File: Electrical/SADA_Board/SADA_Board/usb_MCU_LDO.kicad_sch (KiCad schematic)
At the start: 12 parts, among them J16 USB_B_Micro, Q2 NVR5198NLT1G, Q3 NVR5198NLT1G, U11 RTQ2520GQW, U12 NCV68261MTWAITBG, U13 NCV68261MTWAITBG

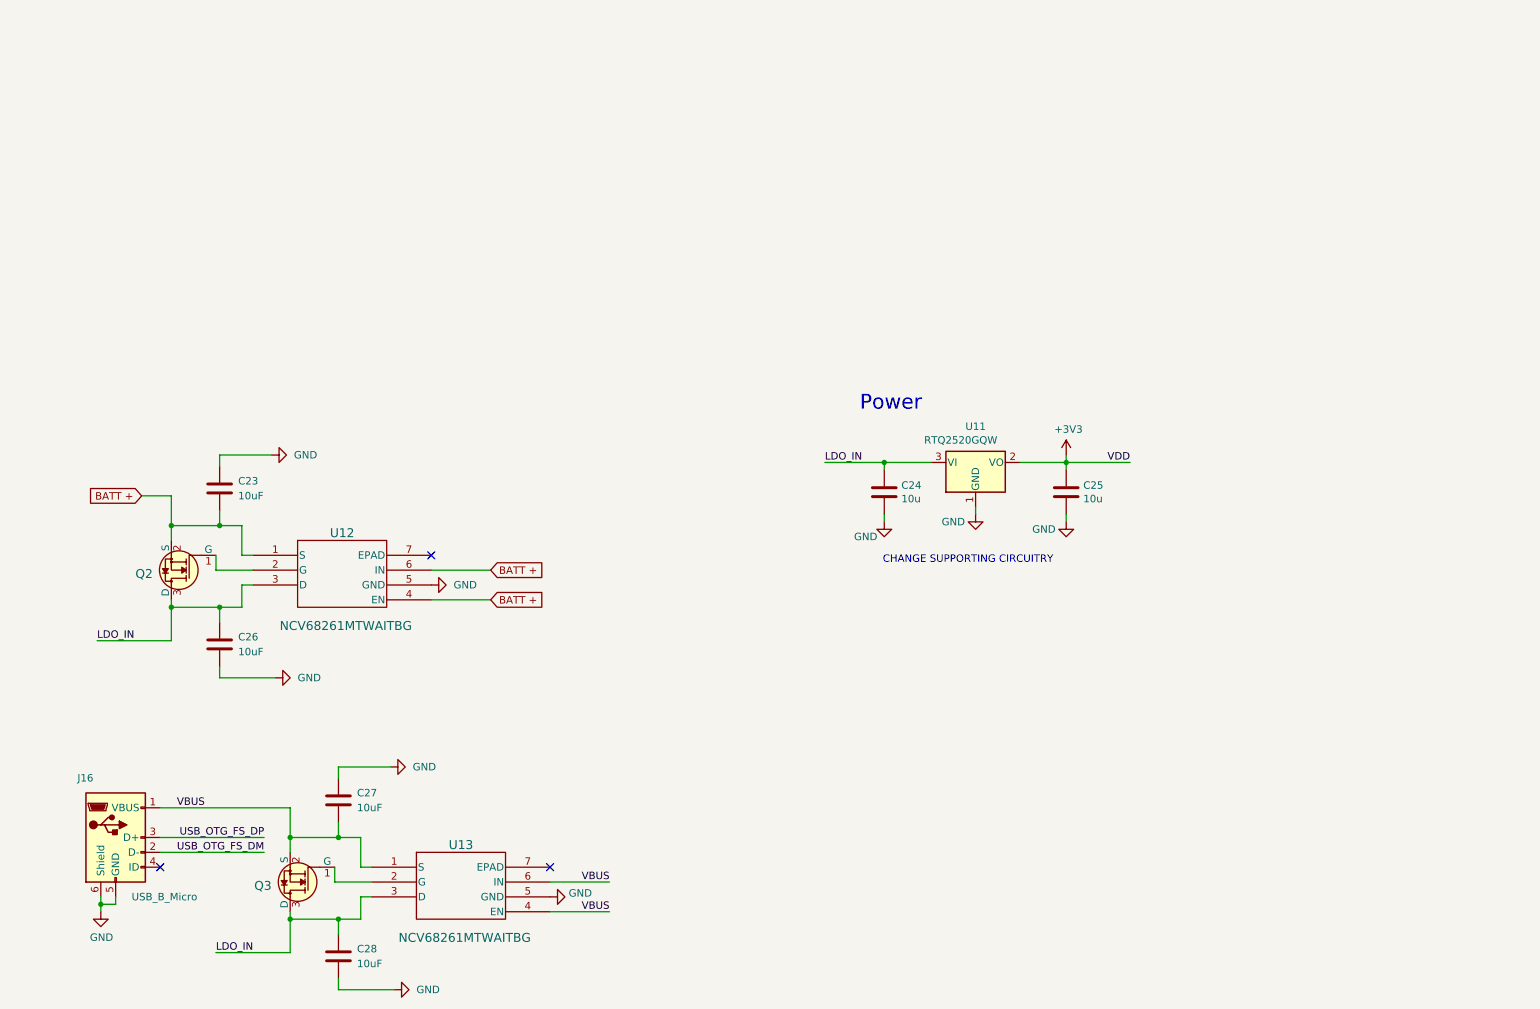
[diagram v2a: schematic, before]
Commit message: Connectors, Oscillator
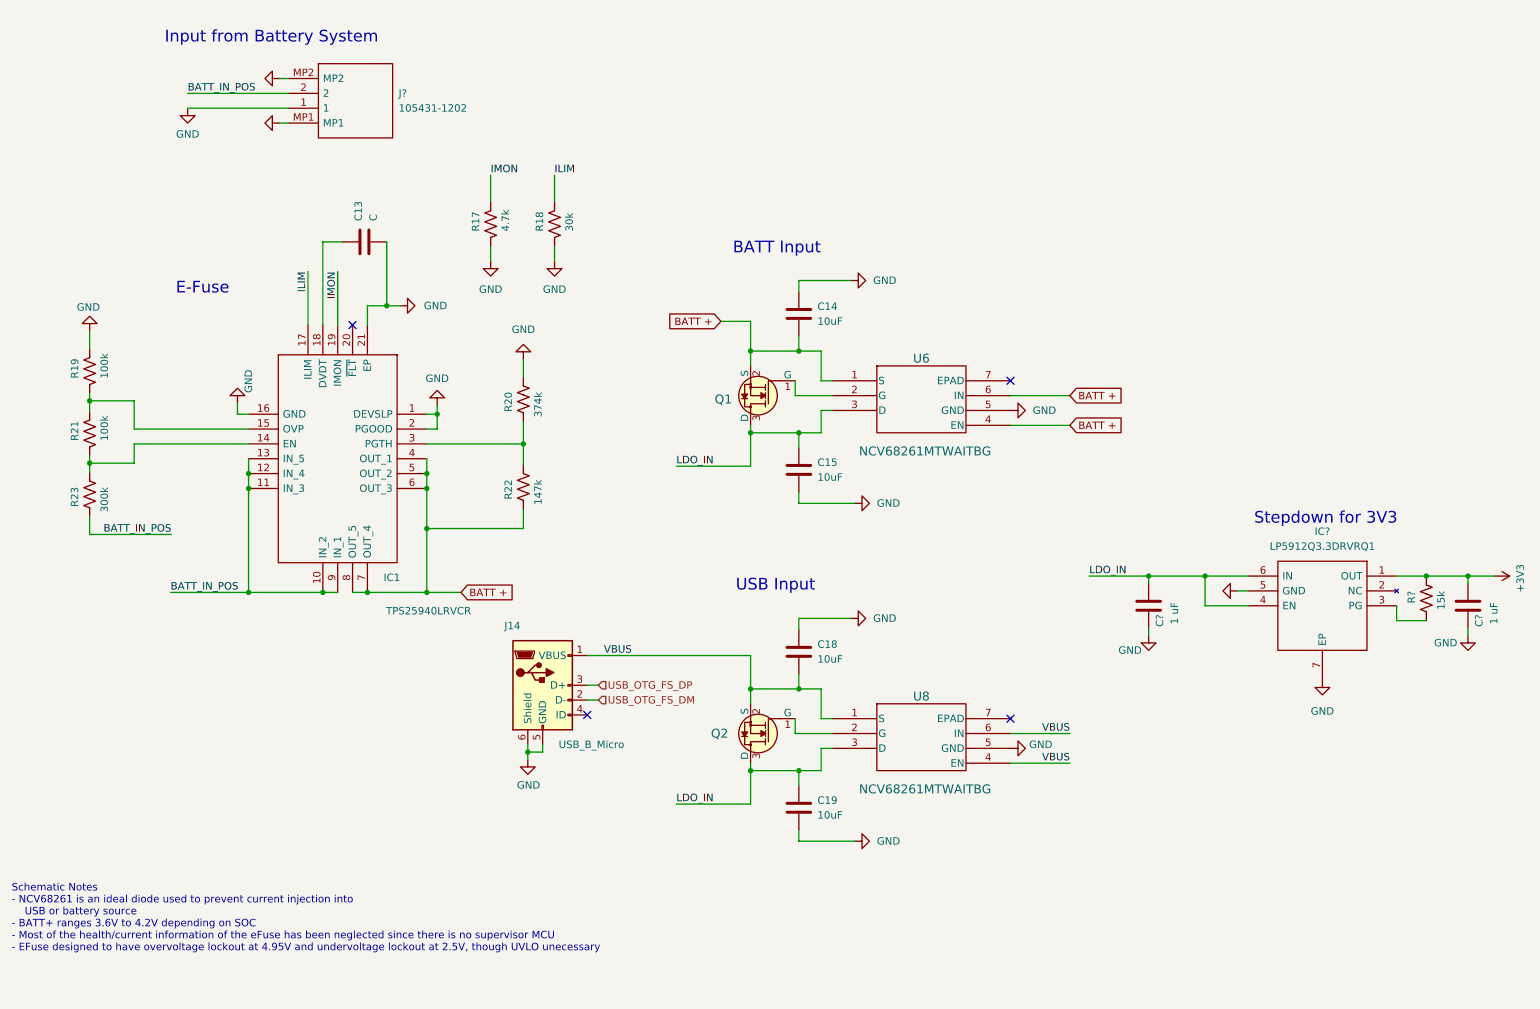
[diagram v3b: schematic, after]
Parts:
- removed C23, C27, C28: 10uF, Capacitor_SMD:C_0603_1608Metric_Pad1.08x0.95mm_HandSolder, symbol Device:C
- removed C24, C25: 10u, Capacitor_SMD:C_0805_2012Metric, symbol Device:C
- removed U11: RTQ2520GQW, symbol Regulator_Linear:NCP1117-3.3_SOT223
- added C13: C, Capacitor_SMD:C_0402_1005Metric, symbol Device:C
- added C14, C18, C19: 10uF, Capacitor_SMD:C_0603_1608Metric, symbol Device:C
- added C? (x2): 1 uF, Capacitor_SMD:C_0603_1608Metric, symbol Device:C
- added IC1: TPS25940LRVCR, QFN50P300X400X80-21N, symbol TPS25940LRVCR:TPS25940LRVCR
- added IC?: LP5912Q3.3DRVRQ1, SON65P200X200X80-7N, symbol LP5912Q3.3DRVRQ1:LP5912Q3.3DRVRQ1
- added J?: 105431-1202, Miles Added:1054311202, symbol molex_105431-1202:105431-1202
- added R17: 4.7k, Resistor_SMD:R_0402_1005Metric, symbol Device:R_US
- added R18: 30k, Resistor_SMD:R_0402_1005Metric, symbol Device:R_US
- added R19, R21: 100k, Resistor_SMD:R_0402_1005Metric, symbol Device:R_US
- added R20: 374k, Resistor_SMD:R_0402_1005Metric, symbol Device:R_US
- added R22: 147k, Resistor_SMD:R_0402_1005Metric, symbol Device:R_US
- added R23: 300k, Resistor_SMD:R_0402_1005Metric, symbol Device:R_US
- added R?: 15k, Resistor_SMD:R_0603_1608Metric, symbol Device:R_US
- C15: renamed from C26; footprint Capacitor_SMD:C_0603_1608Metric_Pad1.08x0.95mm_HandSolder -> Capacitor_SMD:C_0603_1608Metric
- renumbered J16 to J14, Q2 to Q1, Q3 to Q2, U12 to U6, U13 to U8
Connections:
- net +3V3: now also C?.2, IC?.1 (OUT), R?.2
- net BATT +: now also C14.2, IC1.4 (OUT_1), IC1.5 (OUT_2), IC1.6 (OUT_3), IC1.7 (OUT_4), IC1.8 (OUT_5), R22.1
- net GND: now also C13.2, C14.1, C18.1, C19.2, C?.1, C?.1, IC1.1 (DEVSLP), IC1.16 (GND), IC1.2 (PGOOD), IC1.21 (EP), IC?.5 (GND), IC?.7 (EP), J?.1, J?.MP1, J?.MP2, R17.2, R18.2, R19.1, R20.2
- net LDO_IN: now also C19.1, C?.2, IC?.4 (EN), IC?.6 (IN)
- net VBUS: now also C18.2
- new net: C13.1, IC1.18 (DVDT)
- new net: IC1.15 (OVP), R19.2, R21.1
- new net: IC1.14 (EN), R21.2, R23.2
- new net: IC1.3 (PGTH), R20.1, R22.2
- new net: IC?.3 (PG), R?.1
- new net BATT_IN_POS: IC1.10 (IN_2), IC1.11 (IN_3), IC1.12 (IN_4), IC1.13 (IN_5), IC1.9 (IN_1), J?.2, R23.1
- new net ILIM: IC1.17 (ILIM), R18.1
- new net IMON: IC1.19 (IMON), R17.1
- no-connect marks 3 -> 4
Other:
- note added: "BATT Input"
- note added: "E-Fuse"
- note added: "Input from Battery System"
- note added: "Schematic Notes - NCV68261 is an ideal diode used to prevent current injection into USB or battery source - BATT+ ranges 3.6V to 4.2V depending on SOC - Most of the health/current information of the eFuse has been neglected since there is no supervisor MCU - EFuse designed to have overvoltage lockout at 4.95V and undervoltage lockout at 2.5V, though UVLO unecessary"
- note added: "Stepdown for 3V3"
- note added: "USB Input"
- note removed: "CHANGE SUPPORTING CIRCUITRY"
- note removed: "Power"
- moved on the sheet: C15, J14, Q1, Q2, U6, U8

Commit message: Pre-Design Review II
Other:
- note added: "Ideal Diode"
- note added: "Schematic Notes - NCV68261 is an ideal diode used to prevent current injection into USB or battery source - Mimics common two source voltage input selection circuit of having a series diode on each line w/o voltage drop - BATT+ ranges 3.6V to 4.2V depending on SOC - Most of the health/current information of the eFuse has been neglected since there is no supervisor MCU - EFuse designed to have ove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"
- note removed: "Schematic Notes - NCV68261 is an ideal diode used to prevent current injection into USB or battery source - BATT+ ranges 3.6V to 4.2V depending on SOC - Most of the health/current information of the eFuse has been neglected since there is no supervisor MCU - EFuse designed to have overvoltage lockout at 4.95V and undervoltage lockout at 2.5V, though UVLO unecessary"
- moved on the sheet: C13, C14, C15, C18, C19, C?, IC1, IC?, J14, J?, Q1, Q2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

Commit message: Pre-passive retainment change
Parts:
- added EXT?: PWR Banana Plugs, 0_custom:EXT_no_footprint, symbol 0_custom:{lt}name{gt}
- added EXT?: Power Male Connector, 0_custom:EXT_no_footprint, symbol 0_custom:{lt}name{gt}
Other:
- moved on the sheet: C?, IC?, R?

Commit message: pre-gio review
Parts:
- removed J14: USB_B_Micro, Miles Added:USB_Micro-B_Amphenol_10103594-0001LF_Horizontal_modified, symbol RP2040_minimal-rescue:USB_B_Micro-Connector
- removed U6, U8: NCV68261MTWAITBG, WDFNW6_511DW_ONS_OSI, symbol Ideal_diode_NCV:NCV68261MTWAITBG
- added D9: TVS, Diode_SMD:D_0402_1005Metric, symbol Diode:ESD5Zxx
- added J8: 10103594-0001LF, digikey-footprints:USB_Micro_B_Female_10103594-0001LF, symbol dk_USB-DVI-HDMI-Connectors:10103594-0001LF
- added TP10, TP11, TP12, TP7, TP8, TP9: TestPoint, TestPoint:TestPoint_Pad_D1.5mm, symbol Connector:TestPoint
- added U4, U5: NCV68261MTWAITBG, Miles Added:WDFNW6_511DW_ONS_OSI, symbol Ideal_diode_NCV:NCV68261MTWAITBG
- IC1: footprint QFN50P300X400X80-21N -> Miles Added:QFN50P300X400X80-21N
- IC2: renamed from IC?; footprint SON65P200X200X80-7N -> Miles Added:SON65P200X200X80-7N
- R4: renamed from R18; value 30k -> 16.8k; MPN AC0402FR-134K7L -> AC0402FR-0716K9L
- gave numbers to parts that had none: 6
- renumbered C18 to C12, C19 to C13, C13 to C14, C14 to C15, C15 to C16, Q2 to Q1, Q1 to Q2, R23 to R10, R17 to R5, R19 to R6, R20 to R7, R21 to R8, R22 to R9
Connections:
- net +3V3: now also TP11.1
- net BATT +: now also TP9.1, U5.1 (S), U5.4 (EN), U5.6 (IN)
- net BATT_IN_POS: now also TP12.1
- net GND: now also D9.2 (A), J8.5, J8.SH, TP8.1, U4.5 (GND), U4.7 (EPAD), U5.5 (GND), U5.7 (EPAD)
- net LDO_IN: now also D9.1 (K), TP10.1, U4.3 (D), U5.3 (D)
- net USB_OTG_FS_DM: now also J8.2
- net USB_OTG_FS_DP: now also J8.3
- net VBUS: now also J8.1, TP7.1, U4.1 (S), U4.4 (EN), U4.6 (IN)
- net at Q2.1 (G): now also U5.2 (G)
- net at Q1.1 (G): now also U4.2 (G)
- no-connect marks 4 -> 2
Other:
- note added: "BATT Ideal Diode"
- note added: "BATT eFuse"
- note removed: "BATT Input"
- note removed: "E-Fuse"
- moved on the sheet: C12, C13, C15, C16, C17, C18, EXT6, EXT7, IC2, Q1, Q2, R11

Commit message: ESD changes
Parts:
- added C33: 100nF, Capacitor_SMD:C_0402_1005Metric, symbol Device:C
- added U11: USBLC6-2SC6, Package_TO_SOT_SMD:SOT-23-6, symbol Power_Protection:USBLC6-2SC6
- TP10, TP11, TP12, TP7, TP8, TP9: footprint TestPoint:TestPoint_Pad_D1.5mm -> TestPoint:TestPoint_Pad_D1.0mm
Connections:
- net GND: now also C33.2, U11.2 (GND)
- net USB_OTG_FS_DM: now also U11.6 (I/O1); no longer J8.2
- net USB_OTG_FS_DP: now also U11.4 (I/O2); no longer J8.3
- net VBUS: now also C33.1, U11.5 (VBUS); no longer C12.2, Q1.2 (S), TP7.1, U4.1 (S)
- new net: C12.2, Q1.2 (S), TP7.1, U4.1 (S)
- new net USB_CONN_DM: J8.2, U11.1 (I/O1)
- new net USB_CONN_DP: J8.3, U11.3 (I/O2)
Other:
- moved on the sheet: C12, C13, J8, Q1, TP7, U4

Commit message: layout prog
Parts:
- added C34: 22 uF, Capacitor_SMD:C_1210_3225Metric, symbol Device:C
- added C35: 100nF, Capacitor_SMD:C_0402_1005Metric, symbol Device:C
- added D4, D5: TVS, Diode_SMD:D_0402_1005Metric, symbol Diode:ESD5Zxx
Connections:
- net BATT +: now also C34.1, D5.1 (K)
- net BATT_IN_POS: now also C35.2, D4.1 (K)
- net GND: now also C34.2, C35.1, D4.2 (A), D5.2 (A)
- net VBUS: now also C12.2, Q1.2 (S), TP7.1, U4.1 (S)
